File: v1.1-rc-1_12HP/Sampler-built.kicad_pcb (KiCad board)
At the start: 4 copper layers, 60.5 x 109.2 mm, 231 parts, among them J10 Eurorack_Power_10pin_Unshroud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, J11 3.5mm_Mono_Switched, J12 3.5mm_Mono_Switched, J13 3.5mm_Mono_Switched, J14 3.5mm_Mono_Switched, J15 3.5mm_Mono_Switched, J16 3.5mm_Mono_Switched, J17 3.5mm_Mono_Switched, J2 3.5mm_Mono_Switched, J3 Conn_01x04, J4 Conn_02x04, J6 3.5mm_Mono_Switched, J7 3.5mm_Mono_Switched, J8 3.5mm_Mono_Switched, J9 3.5mm_Mono_Switched, U1 TL072H, U10 TL072H, U11 TL072H, U12 TL072H, U13 AP62200WU-7, U14 TL072H, U15 NJM2068, U16 NJM2068, U2 STM32F746IE, U3 TL072H, U4 SDRAM_IS42S16400J-6BLI-TR, U5 TL072H, U6 NCP51460SN33, U8 TL072H, U9 PCM3060PW, Y1 16MHz_18pF_FA238

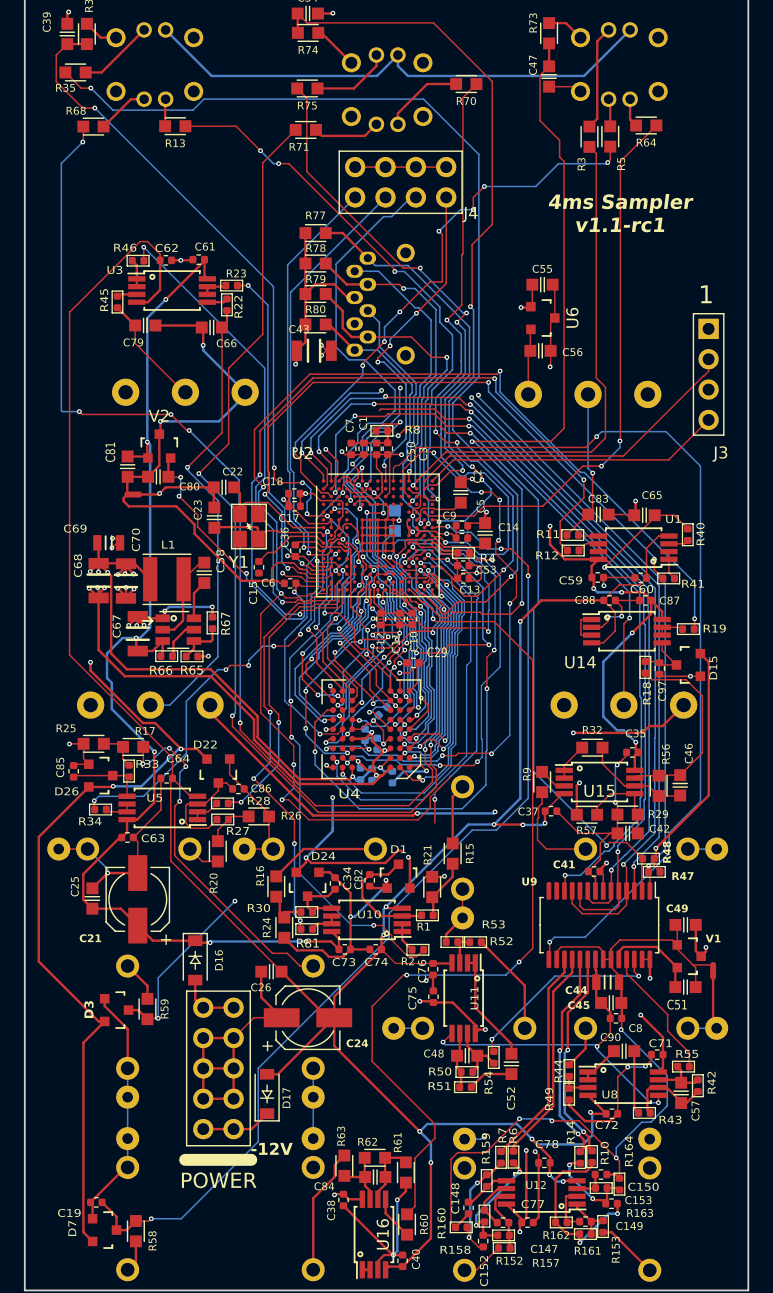
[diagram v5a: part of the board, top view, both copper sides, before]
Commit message: Updates to pcb / routing for noise mitigation
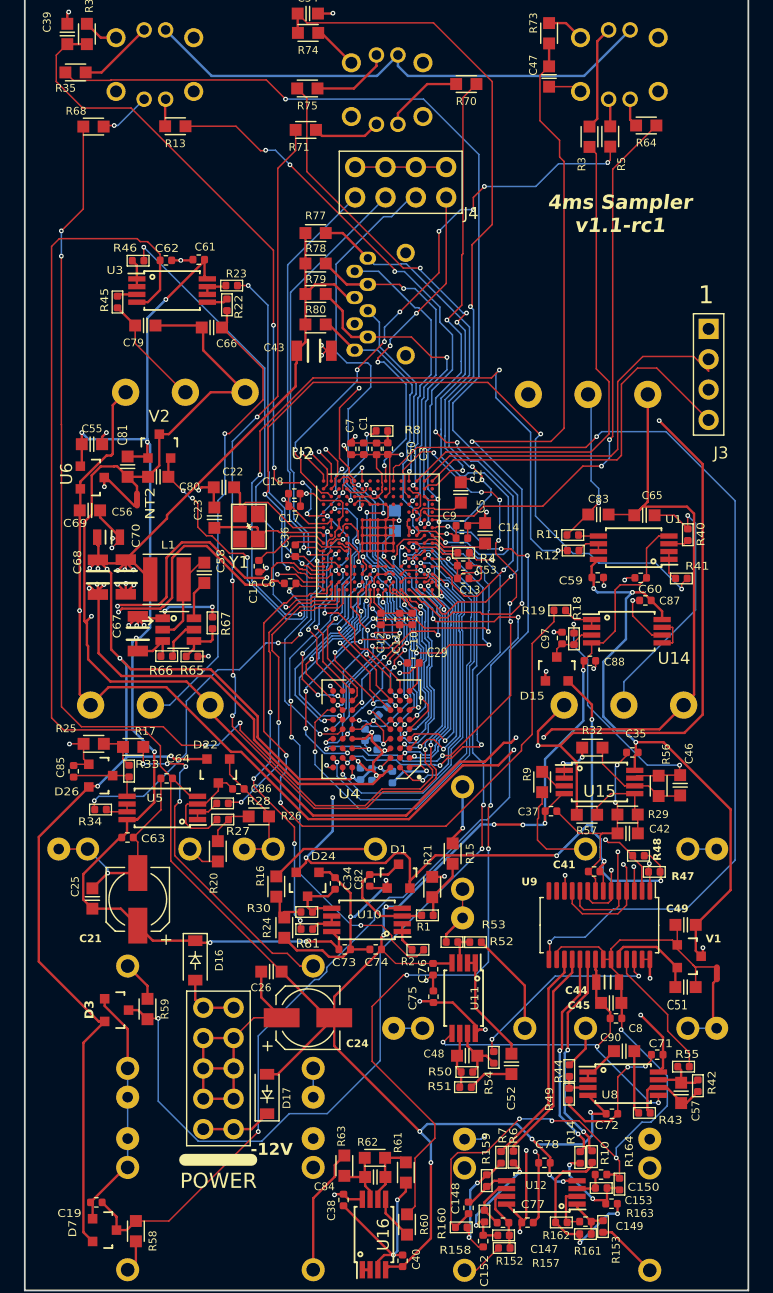
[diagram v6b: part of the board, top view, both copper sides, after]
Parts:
- moved C55 40.0 mm to (141.3, 54.7)
- moved C56 40.0 mm to (141.1, 60.2)
- moved U6 40.0 mm to (141.3, 57.5)
- moved D15 11.0 mm to (180.2, 73.5), turned to 0 degrees
- moved R19 10.9 mm to (180.4, 68.6), turned to 180 degrees
- moved C97 8.57 mm to (180.6, 70.9), turned to 90 degrees
- moved R18 6.43 mm to (181.6, 71.0), turned to -90 degrees
- moved C88 5.32 mm to (182.9, 72.8)
- moved R41 1.06 mm to (190.6, 65.9), turned to 0 degrees
- moved R48 0.87 mm to (187.0, 89.2)
- moved NT2 0.52 mm to (145.0, 59.3), turned to -90 degrees
- moved C69 0.47 mm to (142.7, 62.5)
- moved NT1 0.37 mm to (193.6, 99.0)
- moved C70 0.34 mm to (144.1, 65.8)
- moved C68 0.29 mm to (141.8, 65.8)
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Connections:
- R19 pad 1: Net-(U14B--) -> Net-(U14A--)
- U14 pad 1: Net-(U14A-+) -> Net-(U14A--)
- U14 pad 2: GND -> Net-(U14A--)
- U14 pad 3: Net-(U14A-+) -> Net-(D15-AK)
- U14 pad 5: Net-(D15-AK) -> Net-(U14B-+)
- U14 pad 6: Net-(U14B--) -> GND
- U14 pad 7: Net-(U14B--) -> Net-(U14B-+)
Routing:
- net /A2: track 107.7 -> 59.9 mm, vias 6 -> 2
- net /D13: track 44.3 -> 83.9 mm
- net +3V3: track 366.5 -> 387.2 mm
- net GND: track 372.5 -> 362.3 mm, vias 54 -> 59
- net /SD-NE1: track 52.3 -> 43.6 mm, vias 4 -> 2
- net /SWDIO: track 25.2 -> 32.3 mm
- net /A7: track 59.3 -> 65.9 mm
- net /CODEC_RESET: track 77.2 -> 83.2 mm
- net Net-(C46-Pad1): track 16.8 -> 22.4 mm, vias 0 -> 2
- net GNDADC: track 173.4 -> 168.6 mm, vias 6 -> 4
- net /BOOT0: track 13.2 -> 8.76 mm
- net /SWDCLK: track 28.6 -> 32.9 mm
- net /D7: track 100.9 -> 104.9 mm, vias 7 -> 6
- net VREF+: track 159.5 -> 163.3 mm, vias 2 -> 7
- net Net-(U14A--): track 0.00 -> 3.15 mm
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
